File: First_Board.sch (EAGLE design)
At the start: 54 parts, among them U0 F22X4---DA38, U1 TLC59108PW, U3 A1101, U4 TPS62111RSA

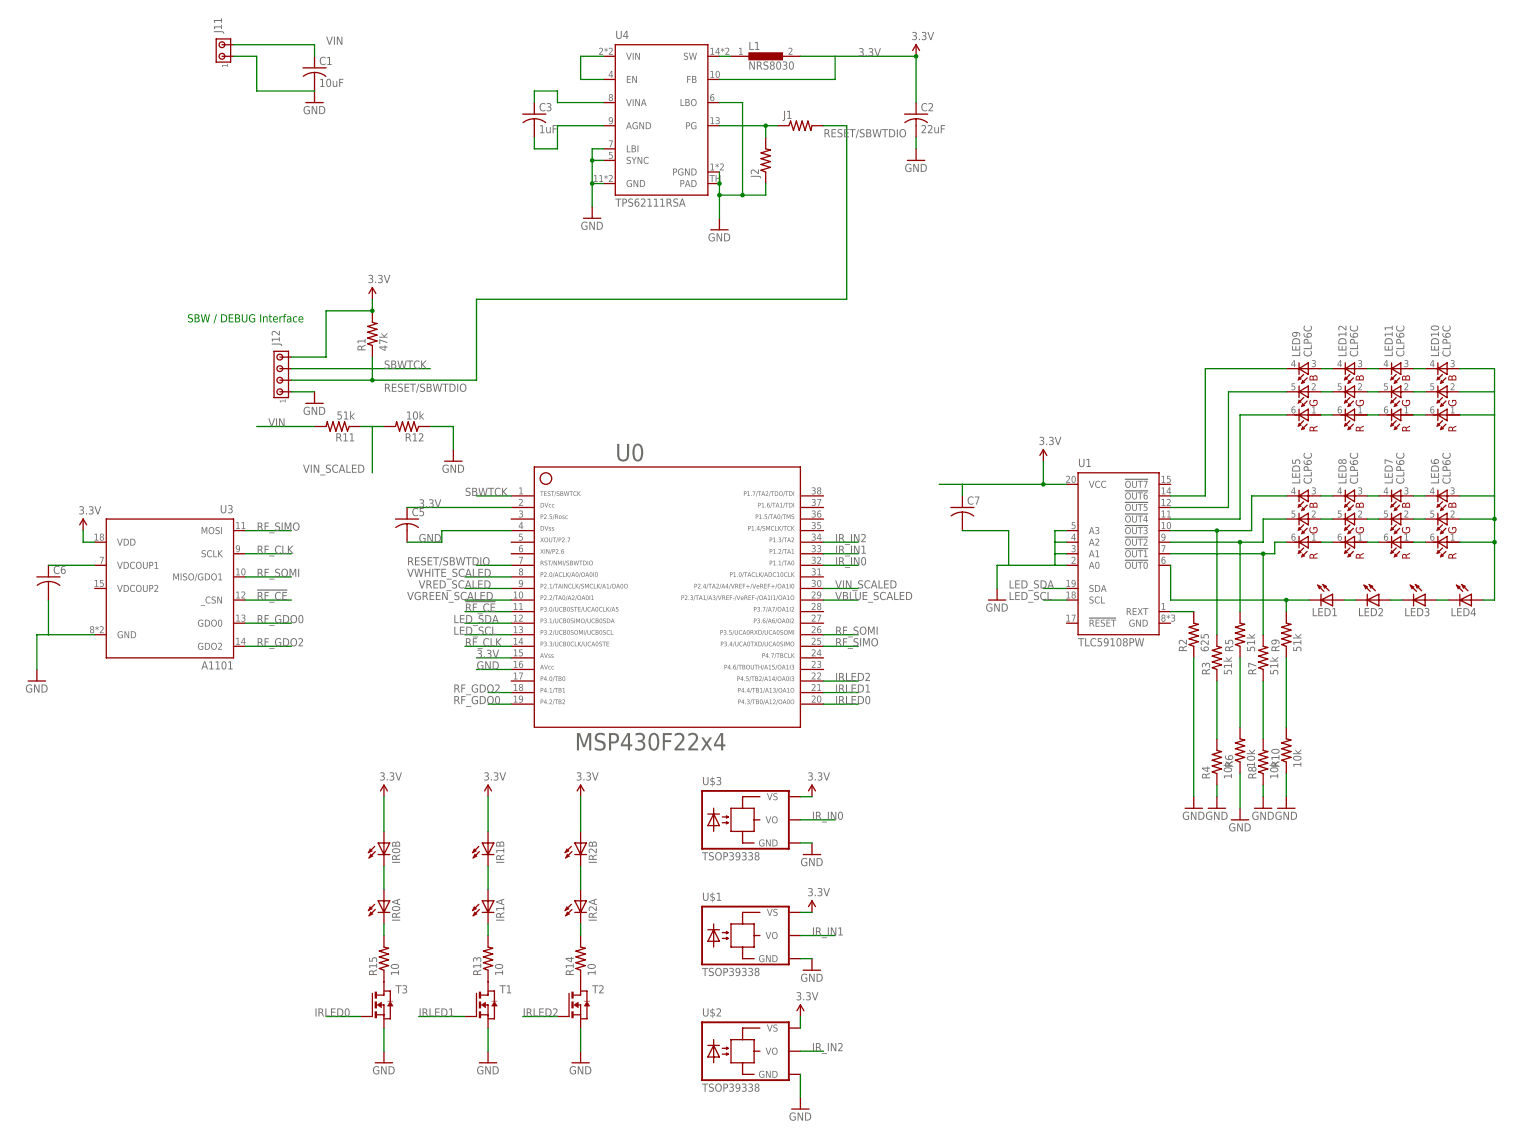
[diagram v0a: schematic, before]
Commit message: Adding rectifier bridge to schematic
git-svn-id: file:///p/svn/Projects/Boards/Driveway_Lights@66 1e7840b9-f7c2-db11-b69c-00d0b71b9132
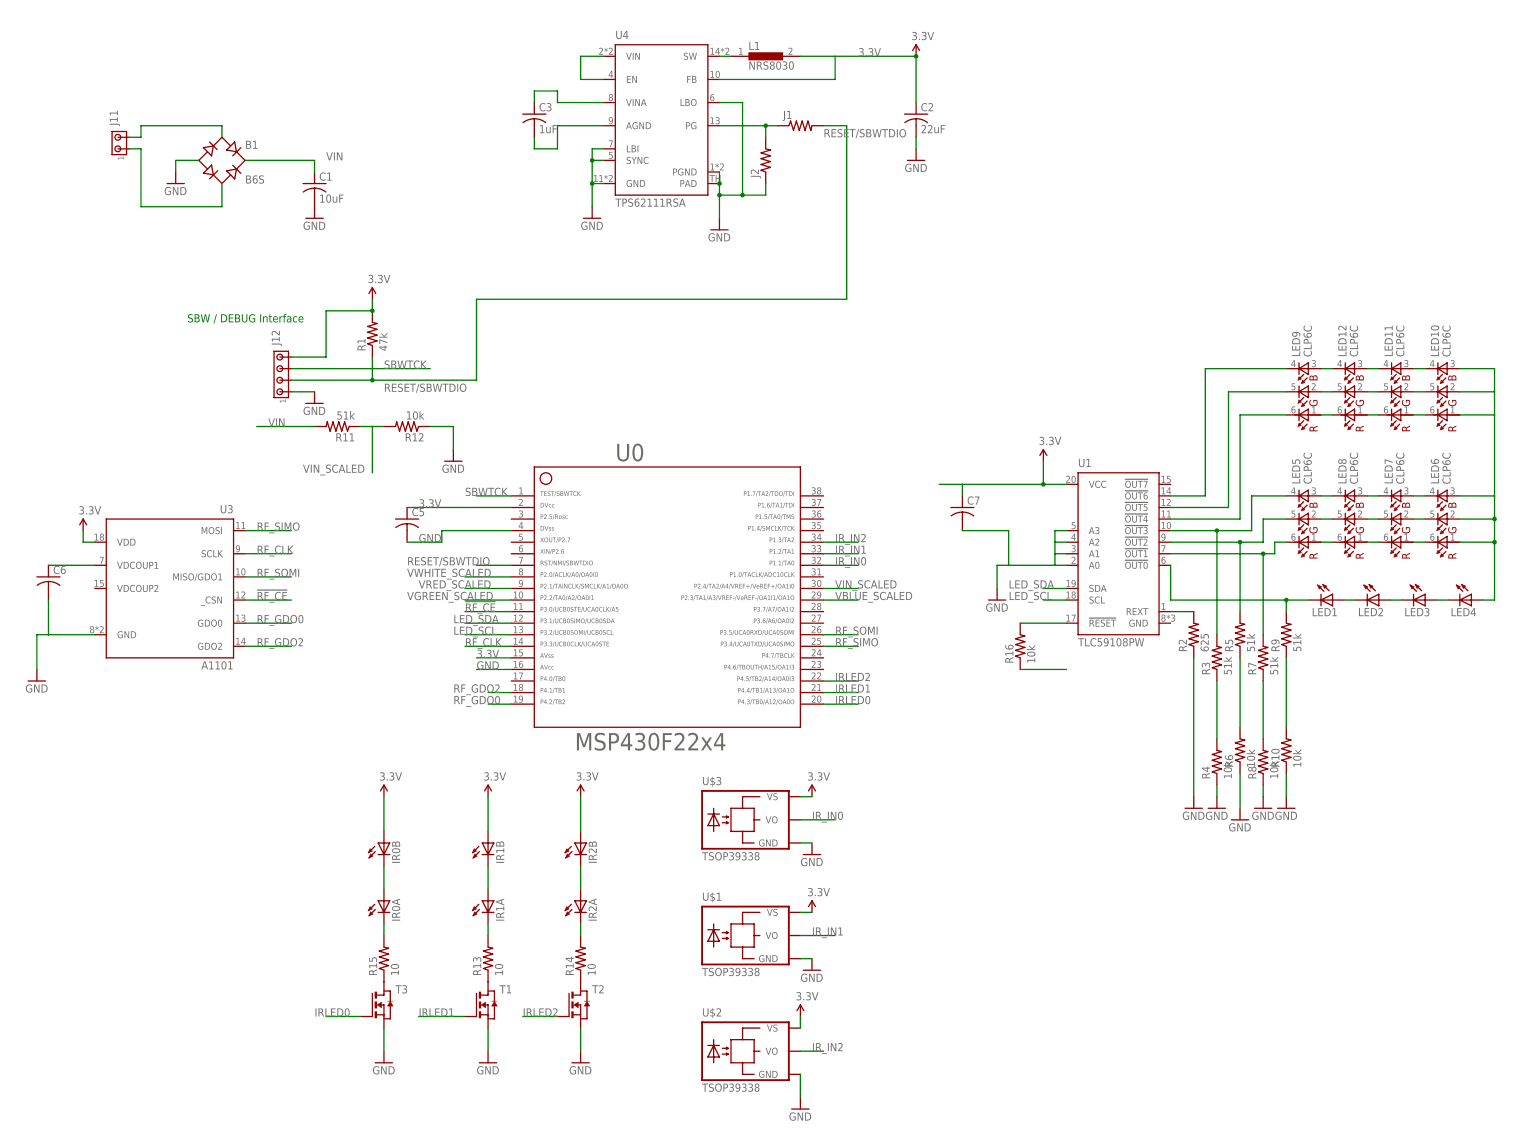
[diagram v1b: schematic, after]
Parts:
- added B1: B6S, rectifier:B6S
- added R16: 10k, rcl:R-US_R0603
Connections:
- new net N$38: R16.2, U1.!RESET
- new net N$39: B1.AC1, J11.2
- new net N$40: B1.AC2, J11.1
- net 3.3V: now also R16.1
- net GND: now also B1.-; no longer J11.1
- net VIN: now also B1.+; no longer J11.2
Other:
- moved on the sheet: C1, J11
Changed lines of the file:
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@@
 <part name="P+10" library="SparkFun" deviceset="3.3V" device=""/>
 <part name="GND19" library="supply1" deviceset="GND" device=""/>
+<part name="R16" library="rcl" deviceset="R-US_" device="R0603" value="10k"/>
+<part name="B1" library="rectifier" deviceset="B*S" device="" technology="6"/>
+<part name="GND20" library="supply1" deviceset="GND" device=""/>
 </parts>
 <sheets>
@@
 <instance part="U4" gate="G$1" x="5.08" y="104.14"/>
 <instance part="L1" gate="G$1" x="30.48" y="111.76"/>
-<instance part="C1" gate="G$1" x="-68.58" y="109.22"/>
+<instance part="C1" gate="G$1" x="-68.58" y="83.82"/>
 <instance part="C2" gate="G$1" x="63.5" y="99.06"/>
 <instance part="C3" gate="G$1" x="-20.32" y="99.06"/>
@@
 <instance part="GND2" gate="1" x="20.32" y="73.66"/>
 <instance part="GND3" gate="1" x="63.5" y="88.9"/>
-<instance part="GND4" gate="1" x="-68.58" y="101.6"/>
+<instance part="GND4" gate="1" x="-68.58" y="76.2"/>
 <instance part="J1" gate="G$1" x="38.1" y="96.52"/>
 <instance part="U3" gate="G$1" x="-99.06" y="-5.08" rot="MR0"/>
@@
 <instance part="R11" gate="G$1" x="-63.5" y="30.48" rot="R180"/>
 <instance part="R12" gate="G$1" x="-48.26" y="30.48" rot="R180"/>
-<instance part="J11" gate="G$1" x="-88.9" y="111.76" rot="R90"/>
+<instance part="J11" gate="G$1" x="-111.76" y="91.44" rot="R90"/>
 <instance part="J12" gate="G$1" x="-76.2" y="40.64" rot="R90"/>
 <instance part="GND11" gate="1" x="-68.58" y="35.56"/>
@@
 <instance part="P+10" gate="G$1" x="40.64" y="-50.8"/>
 <instance part="GND19" gate="1" x="40.64" y="-63.5"/>
+<instance part="R16" gate="G$1" x="86.36" y="-17.78" rot="R90"/>
+<instance part="B1" gate="G$1" x="-88.9" y="88.9"/>
+<instance part="GND20" gate="1" x="-99.06" y="83.82"/>
 </instances>
 <busses>
@@
 <pinref part="C1" gate="G$1" pin="2"/>
 <pinref part="GND4" gate="1" pin="GND"/>
-<wire x1="-68.58" y1="104.14" x2="-81.28" y2="104.14" width="0.1524" layer="91"/>
-<wire x1="-81.28" y1="104.14" x2="-81.28" y2="111.76" width="0.1524" layer="91"/>
-<pinref part="J11" gate="G$1" pin="1"/>
-<wire x1="-81.28" y1="111.76" x2="-86.36" y2="111.76" width="0.1524" layer="91"/>
 </segment>
 <segment>
@@
 <wire x1="40.64" y1="-60.96" x2="38.1" y2="-60.96" width="0.1524" layer="91"/>
 <pinref part="U$3" gate="G$1" pin="GND"/>
+</segment>
+<segment>
+<pinref part="B1" gate="G$1" pin="-"/>
+<wire x1="-93.98" y1="88.9" x2="-99.06" y2="88.9" width="0.1524" layer="91"/>
+<pinref part="GND20" gate="1" pin="GND"/>
+<wire x1="-99.06" y1="88.9" x2="-99.06" y2="86.36" width="0.1524" layer="91"/>
 </segment>
 </net>
@@
 </segment>
 <segment>
-<pinref part="J11" gate="G$1" pin="2"/>
 <pinref part="C1" gate="G$1" pin="1"/>
-<wire x1="-68.58" y1="111.76" x2="-68.58" y2="114.3" width="0.1524" layer="91"/>
-<wire x1="-68.58" y1="114.3" x2="-86.36" y2="114.3" width="0.1524" layer="91"/>
-<label x="-66.04" y="114.3" size="1.778" layer="95"/>
+<wire x1="-68.58" y1="86.36" x2="-68.58" y2="88.9" width="0.1524" layer="91"/>
+<label x="-66.04" y="88.9" size="1.778" layer="95"/>
+<pinref part="B1" gate="G$1" pin="+"/>
+<wire x1="-83.82" y1="88.9" x2="-68.58" y2="88.9" width="0.1524" layer="91"/>
 </segment>
 <segment>
@@
 <pinref part="U$3" gate="G$1" pin="VS"/>
 </segment>
+<segment>
+<pinref part="R16" gate="G$1" pin="1"/>
+<wire x1="86.36" y1="-22.86" x2="96.52" y2="-22.86" width="0.1524" layer="91"/>
+</segment>
 </net>
 <net name="SBWTCK" class="0">
@@
 </segment>
 </net>
+<net name="N$38" class="0">
+<segment>
+<pinref part="U1" gate="G$1" pin="!RESET"/>
+<pinref part="R16" gate="G$1" pin="2"/>
+<wire x1="96.52" y1="-12.7" x2="86.36" y2="-12.7" width="0.1524" layer="91"/>
+</segment>
+</net>
+<net name="N$39" class="0">
+<segment>
+<pinref part="B1" gate="G$1" pin="AC1"/>
+<wire x1="-88.9" y1="93.98" x2="-88.9" y2="96.52" width="0.1524" layer="91"/>
+<wire x1="-88.9" y1="96.52" x2="-106.68" y2="96.52" width="0.1524" layer="91"/>
+<wire x1="-106.68" y1="96.52" x2="-106.68" y2="93.98" width="0.1524" layer="91"/>
+<pinref part="J11" gate="G$1" pin="2"/>
+<wire x1="-106.68" y1="93.98" x2="-109.22" y2="93.98" width="0.1524" layer="91"/>
+</segment>
+</net>
+<net name="N$40" class="0">
+<segment>
+<pinref part="J11" gate="G$1" pin="1"/>
+<wire x1="-109.22" y1="91.44" x2="-106.68" y2="91.44" width="0.1524" layer="91"/>
+<wire x1="-106.68" y1="91.44" x2="-106.68" y2="78.74" width="0.1524" layer="91"/>
+<wire x1="-106.68" y1="78.74" x2="-88.9" y2="78.74" width="0.1524" layer="91"/>
+<pinref part="B1" gate="G$1" pin="AC2"/>
+<wire x1="-88.9" y1="78.74" x2="-88.9" y2="83.82" width="0.1524" layer="91"/>
+</segment>
+</net>

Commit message: Schematic review with V
git-svn-id: file:///p/svn/Projects/Boards/Driveway_Lights@67 1e7840b9-f7c2-db11-b69c-00d0b71b9132
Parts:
- removed R16: 10k, rcl:R-US_R0603
- added C10, C4, C8, C9: (no value), rcl:C-USC0603
- added C11: 22uF, rcl:C-USC1210
- added L2: (no value), rcl:R-US_R0603
- C1: value 10uF -> 1uF
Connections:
- net N$11 renamed VDCOUP1
- new net N$42: L2.2, U3.VDD
- new net VDCOUP2: C4.1, U3.VDCOUP2
- net 3.3V: now also C10.1, C8.1, C9.1, L2.1; no longer R16.1, U3.VDD
- net GND: now also C10.2, C11.2, C4.2, C8.2, C9.2, U1.GND
- net N$38: no longer R16.2
- net N$7: now also U0.38; no longer C3.1, U4.VINA
- net VIN: now also C11.1, C3.1, U4.VINA
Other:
- moved on the sheet: C1
